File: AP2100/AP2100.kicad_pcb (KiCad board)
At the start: 6 copper layers, 150 x 150 mm, 73 parts, among them IC1 FDS86242, J1 Bus_PCI_Express_Mini, J2 Bus_PCI_Express_Mini, J3 Bus_PCI_Express_Mini, Q1 HMHA2801AR2, U1 TPS23751PWP, U2 TL431DBV, U3 LS1043ASE7KQB, U4 MPQ8634AGLE-P, U5 MPQ8634AGLE-P

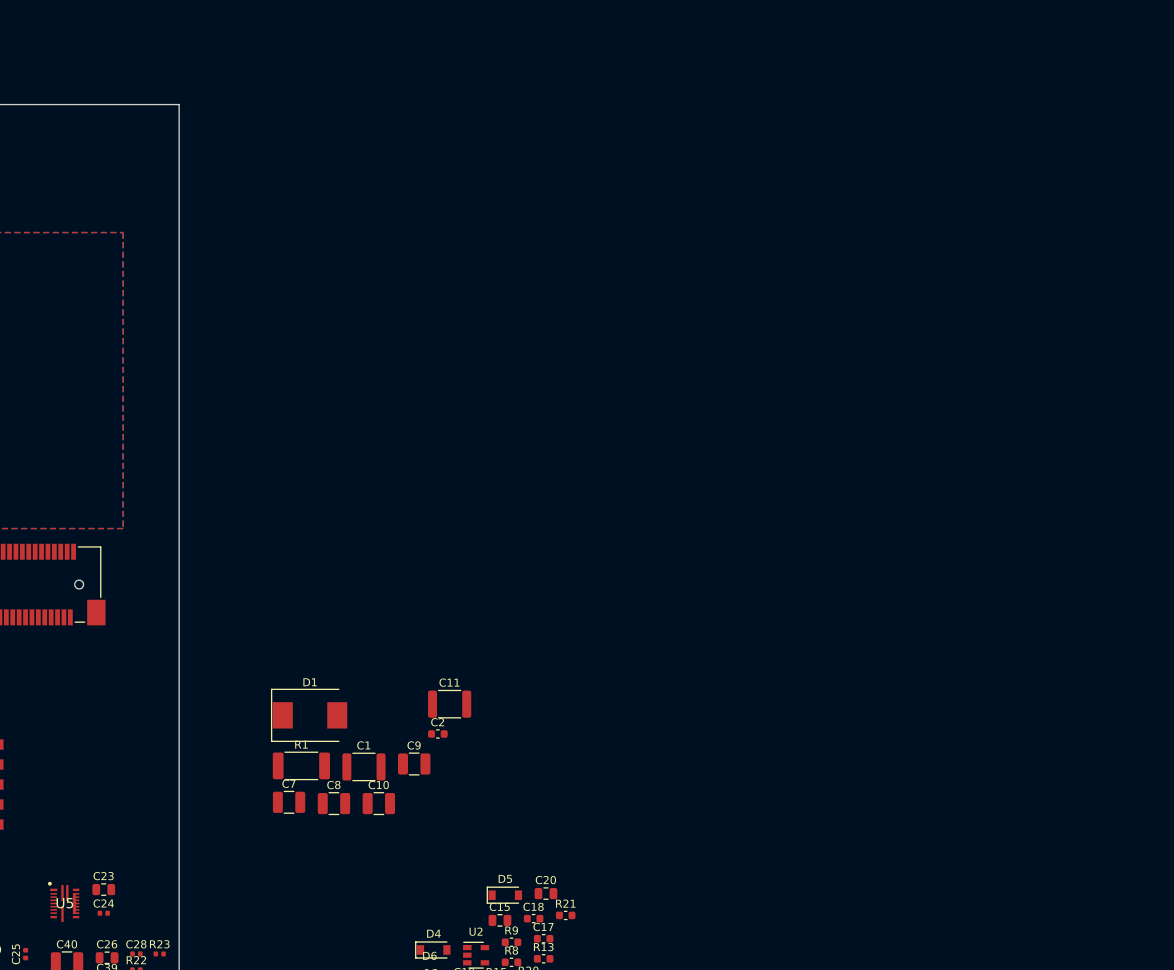
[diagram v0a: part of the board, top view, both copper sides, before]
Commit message: Update PoE section - almost done
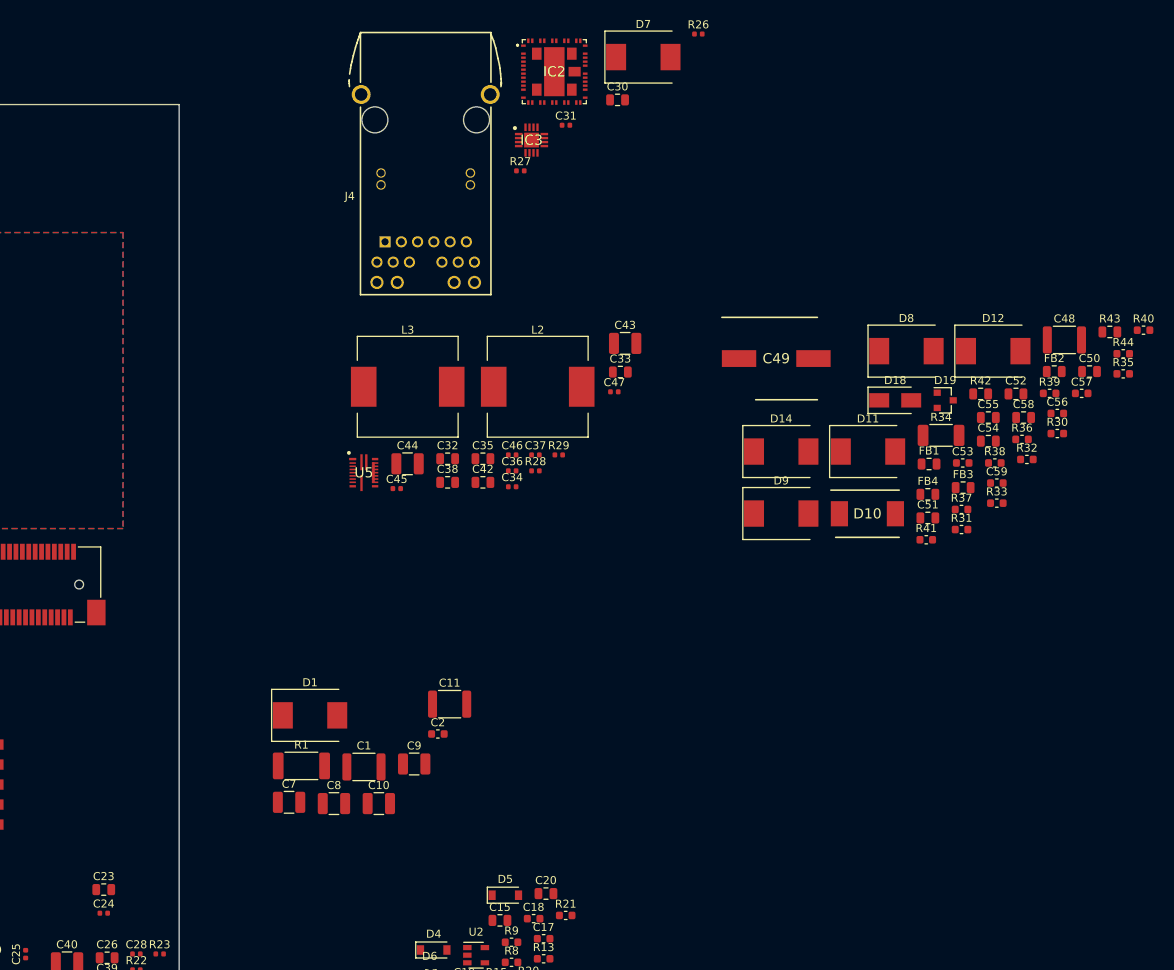
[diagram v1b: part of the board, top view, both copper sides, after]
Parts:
- added C30: 1nF 250V, Capacitor_SMD:C_0805_2012Metric, F.Cu at (204.8, -0.58)
- added C31: .1, Capacitor_SMD:C_0402_1005Metric, F.Cu at (198.4, 2.59)
- added C32: 22uF, Capacitor_SMD:C_0805_2012Metric, F.Cu at (183.6, 44.3)
- added C33: 22uF, Capacitor_SMD:C_0805_2012Metric, F.Cu at (205.2, 33.4)
- added C34: 500pF, Capacitor_SMD:C_0402_1005Metric, F.Cu at (191.6, 47.8)
- added C35: 22uF, Capacitor_SMD:C_0805_2012Metric, F.Cu at (188.0, 44.3)
- added C36: .1uF, Capacitor_SMD:C_0402_1005Metric, F.Cu at (191.6, 45.8)
- added C37: .1uF, Capacitor_SMD:C_0402_1005Metric, F.Cu at (194.5, 43.8)
- added C38: 22uF, Capacitor_SMD:C_0805_2012Metric, F.Cu at (183.6, 47.2)
- added C42: 22uF, Capacitor_SMD:C_0805_2012Metric, F.Cu at (188.0, 47.2)
- added C43: 100uF, Capacitor_SMD:C_1210_3225Metric, F.Cu at (205.8, 29.9)
- added C44: 100uF, Capacitor_SMD:C_1210_3225Metric, F.Cu at (178.6, 44.9)
- added C45: .1uF, Capacitor_SMD:C_0402_1005Metric, F.Cu at (177.2, 48.0)
- added C46: .1uF, Capacitor_SMD:C_0402_1005Metric, F.Cu at (191.6, 43.8)
- added C47: .1uF, Capacitor_SMD:C_0402_1005Metric, F.Cu at (204.4, 35.9)
- added C48: 2.2nF 2KV, Capacitor_SMD:C_1812_4532Metric, F.Cu at (260.7, 29.4)
- added C49: EEEFK2A330P, LIB_EEEFK2A330P:CAPAE1030X1050N, F.Cu at (224.6, 31.8)
- added C50: 1nF 250V, Capacitor_SMD:C_0805_2012Metric, F.Cu at (263.8, 33.4)
- added C51: 33nF 100V, Capacitor_SMD:C_0805_2012Metric, F.Cu at (243.6, 51.7)
- added C52: 33nF 100V, Capacitor_SMD:C_0805_2012Metric, F.Cu at (254.6, 36.2)
- added C53: 1nF, Capacitor_SMD:C_0603_1608Metric, F.Cu at (247.9, 44.8)
- added C54: 33nF 100V, Capacitor_SMD:C_0805_2012Metric, F.Cu at (251.1, 42.1)
- added C55: 33nF 100V, Capacitor_SMD:C_0805_2012Metric, F.Cu at (251.1, 39.1)
- added C56: 10nF 100V, Capacitor_SMD:C_0603_1608Metric, F.Cu at (259.8, 38.6)
- added C57: 10nF 100V, Capacitor_SMD:C_0603_1608Metric, F.Cu at (262.8, 36.1)
- added C58: 10nF 100V, Capacitor_SMD:C_0805_2012Metric, F.Cu at (255.6, 39.1)
- added C59: 10nF 100V, Capacitor_SMD:C_0603_1608Metric, F.Cu at (252.2, 47.3)
- added D10: STPS4S200S, LIB_STPS4S200S:DIOM8059X265N, F.Cu at (236.0, 51.1)
- added D11: SM15T68CA, Diode_SMD:D_SMC, F.Cu at (236.1, 43.4)
- added D12: SM15T68CA, Diode_SMD:D_SMC, F.Cu at (251.8, 30.8)
- added D14: SM15T68CA, Diode_SMD:D_SMC, F.Cu at (225.3, 43.4)
- added D18: SMAJ58A, Diode_SMD:D_SMA, F.Cu at (239.5, 37.0)
- added D19: BAV70, Package_TO_SOT_SMD:SOT-23, F.Cu at (245.8, 37.0)
- added D7: SM15T68CA, Diode_SMD:D_SMC, F.Cu at (208.0, -5.93)
- added D8: SM15T68CA, Diode_SMD:D_SMC, F.Cu at (240.9, 30.8)
- added D9: SM15T68CA, Diode_SMD:D_SMC, F.Cu at (225.3, 51.1)
- added FB1: 220 OHM, Inductor_SMD:L_0805_2012Metric, F.Cu at (243.7, 44.9)
- added FB2: 220 OHM, Inductor_SMD:L_0805_2012Metric, F.Cu at (259.4, 33.4)
- added FB3: 220 OHM, Inductor_SMD:L_0805_2012Metric, F.Cu at (248.0, 47.9)
- added FB4: 220 OHM, Inductor_SMD:L_0805_2012Metric, F.Cu at (243.6, 48.7)
- added IC2: PM8805TR, PM8805TR:PM8805TR, F.Cu at (196.9, -4.11)
- added IC3: PM8804TR, PM8804TR:QFN50P340X340X90-17N, F.Cu at (194.0, 4.44)
- added J4: 0826-1X1T-GH-F, 0826-1X1T-GH-F:BEL_0826-1X1T-GH-F, F.Cu at (180.8, 1.92)
- added L2: .56uH, Scott:L_13.5x12.5mm_H6mm, F.Cu at (194.8, 35.3)
- added L3: .56uH, Scott:L_13.5x12.5mm_H6mm, F.Cu at (178.6, 35.3)
- added R26: 30.1K, Resistor_SMD:R_0402_1005Metric, F.Cu at (214.9, -8.81)
- added R27: 6.98K, Resistor_SMD:R_0402_1005Metric, F.Cu at (192.7, 8.29)
- added R28: 30.1K, Resistor_SMD:R_0402_1005Metric, F.Cu at (194.5, 45.8)
- added R29: 6.98K, Resistor_SMD:R_0402_1005Metric, F.Cu at (197.5, 43.8)
- added R30: 75, Resistor_SMD:R_0603_1608Metric, F.Cu at (259.8, 41.1)
- added R31: 75, Resistor_SMD:R_0603_1608Metric, F.Cu at (247.8, 53.1)
- added R32: 75, Resistor_SMD:R_0603_1608Metric, F.Cu at (256.0, 44.4)
- added R33: 75, Resistor_SMD:R_0603_1608Metric, F.Cu at (252.2, 49.8)
- added R34: 0, Resistor_SMD:R_2010_5025Metric, F.Cu at (245.2, 41.4)
- added R35: 4.7K, Resistor_SMD:R_0603_1608Metric, F.Cu at (268.0, 33.7)
- added R36: 100K, Resistor_SMD:R_0603_1608Metric, F.Cu at (255.4, 41.9)
- added R37: 10K, Resistor_SMD:R_0603_1608Metric, F.Cu at (247.8, 50.6)
- added R38: 3.9K, Resistor_SMD:R_0603_1608Metric, F.Cu at (252.0, 44.8)
- added R39: 3.9K, Resistor_SMD:R_0603_1608Metric, F.Cu at (258.8, 36.1)
- added R40: 3.9K, Resistor_SMD:R_0603_1608Metric, F.Cu at (270.5, 28.2)
- added R41: 10K, Resistor_SMD:R_0603_1608Metric, F.Cu at (243.4, 54.4)
- added R42: 36.5, Resistor_SMD:R_0805_2012Metric, F.Cu at (250.2, 36.2)
- added R43: 150, Resistor_SMD:R_0805_2012Metric, F.Cu at (266.3, 28.4)
- added R44: 26.1K, Resistor_SMD:R_0603_1608Metric, F.Cu at (268.0, 31.2)
- moved U5 65.6 mm to (173.1, 46.0)
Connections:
- net /Power/+12V renamed 12V
- net /Power/CPU_VDD renamed CPU_VDD
- net /Power/EN_VDD renamed EN_VDD
- net Net-(U4-Pad9) renamed CPU_VDD_PG
- net Net-(U5-Pad8) renamed EN_3V3
- net Net-(U5-Pad9) renamed 3V3_PG
- C10 pad 2: GND -> CPU_GND_SENSE
- C11 pad 2: GND -> CPU_GND_SENSE
- C20 pad 2: GND -> CPU_GND_SENSE
- C21 pad 2: GND -> CPU_GND_SENSE
- C22 pad 2: GND -> CPU_GND_SENSE
- C23 pad 2: GND -> CPU_GND_SENSE
- C25 pad 1: GND -> CPU_GND_SENSE
- C26 pad 1: GND -> CPU_GND_SENSE
- C27 pad 2: GND -> CPU_GND_SENSE
- C28 pad 2: GND -> CPU_GND_SENSE
- C29 pad 1: GND -> CPU_GND_SENSE
- C39 pad 1: GND -> CPU_GND_SENSE
- C40 pad 1: GND -> CPU_GND_SENSE
- C41 pad 1: GND -> CPU_GND_SENSE
- C7 pad 2: GND -> CPU_GND_SENSE
- C8 pad 2: GND -> CPU_GND_SENSE
- C9 pad 2: GND -> CPU_GND_SENSE
- R21 pad 1: GND -> CPU_GND_SENSE
- R22 pad 2: GND -> CPU_GND_SENSE
- R23 pad 1: GND -> CPU_GND_SENSE
- TR1 pad 10: GND -> CPU_GND_SENSE
- TR1 pad 9: GND -> CPU_GND_SENSE
- U2 pad 5: GND -> CPU_GND_SENSE
- U4 pad 11: GND -> CPU_GND_SENSE
- U4 pad 12: GND -> CPU_GND_SENSE
- U4 pad 13: GND -> CPU_GND_SENSE
- U4 pad 14: GND -> CPU_GND_SENSE
- U4 pad 15: GND -> CPU_GND_SENSE
- U4 pad 16: GND -> CPU_GND_SENSE
- U4 pad 17: GND -> CPU_GND_SENSE
- U4 pad 18: GND -> CPU_GND_SENSE
- U4 pad 2: GND -> CPU_GND_SENSE
- U4 pad 6: GND -> CPU_GND_SENSE
- U5 pad 11: GND -> CPU_GND_SENSE
- U5 pad 12: GND -> CPU_GND_SENSE
- U5 pad 13: GND -> CPU_GND_SENSE
- U5 pad 14: GND -> CPU_GND_SENSE
- U5 pad 15: GND -> CPU_GND_SENSE
- U5 pad 16: GND -> CPU_GND_SENSE
- U5 pad 17: GND -> CPU_GND_SENSE
- U5 pad 18: GND -> CPU_GND_SENSE
- U5 pad 2: GND -> CPU_GND_SENSE
- U5 pad 6: Net-(U5-Pad6) -> CPU_GND_SENSE
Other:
- net class Default removed

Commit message: Add partsbox.io bom generator script
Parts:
- added C1: 10nF 25V, Capacitor_SMD:C_0603_1608Metric, F.Cu at (-554.7, -455.1)
- added C10: 100nF 25V, Capacitor_SMD:C_0603_1608Metric, F.Cu at (-539.2, -471.4)
- added C11: 100nF, Capacitor_SMD:C_0603_1608Metric, F.Cu at (-544.9, -466.8)
- added C12: 2.2uF 25V, Capacitor_SMD:C_0603_1608Metric, F.Cu at (-571.6, -439.5)
- added C13: 4.7uF, Capacitor_SMD:C_1210_3225Metric, F.Cu at (-592.3, -438.8)
- added C14: 100nF 25V, Capacitor_SMD:C_0603_1608Metric, F.Cu at (-555.4, -460.1)
- added C15: 100nF 25V, Capacitor_SMD:C_0603_1608Metric, F.Cu at (-577.4, -438.0)
- added C16: EEEFK2A330P, LIB_EEEFK2A330P:CAPAE1030X1050N, F.Cu at (-577.2, -476.8)
- added C17: 4.7uF, Capacitor_SMD:C_1210_3225Metric, F.Cu at (-570.2, -457.1)
- added C18: 4.7uF, Capacitor_SMD:C_1210_3225Metric, F.Cu at (-586.2, -442.2)
- added C19: 2.2uF 25V, Capacitor_SMD:C_0603_1608Metric, F.Cu at (-532.2, -476.8)
- added C2: 4.7uF, Capacitor_SMD:C_1210_3225Metric, F.Cu at (-551.1, -474.6)
- added C20: 4.7uF, Capacitor_SMD:C_1210_3225Metric, F.Cu at (-545.4, -481.0)
- added C3: 4.7uF, Capacitor_SMD:C_1210_3225Metric, F.Cu at (-564.6, -458.3)
- added C31: 22nF, Capacitor_SMD:C_0603_1608Metric, F.Cu at (-571.4, -442.0)
- added C4: 100pF 25V, Capacitor_SMD:C_0603_1608Metric, F.Cu at (-558.7, -453.4)
- added C5: 2.2nF 2KV, Capacitor_SMD:C_1812_4532Metric, F.Cu at (-557.4, -474.0)
- added C6: 2.2nF 2KV, Capacitor_SMD:C_1812_4532Metric, F.Cu at (-598.6, -438.4)
- added C60: 47nF 200V, Capacitor_SMD:C_1206_3216Metric, F.Cu at (-577.8, -454.0)
- added C61: 100pF 50V, Capacitor_SMD:C_0805_2012Metric, F.Cu at (-579.3, -446.7)
- added C62: 2200pF 2KV, Capacitor_SMD:C_1812_4532Metric, F.Cu at (-564.5, -467.1)
- added C63: 100nF 25V, Capacitor_SMD:C_0603_1608Metric, F.Cu at (-554.7, -457.6)
- added C64: 220pF, Capacitor_SMD:C_0603_1608Metric, F.Cu at (-531.9, -479.3)
- added C65: 100pF 50V, Capacitor_SMD:C_0805_2012Metric, F.Cu at (-575.6, -443.7)
- added C66: 1nF, Capacitor_SMD:C_0805_2012Metric, F.Cu at (-559.6, -458.7)
- added C67: 47uF 16V, Capacitor_SMD:C_1210_3225Metric, F.Cu at (-580.6, -442.2)
- added C68: 47uF 16V, Capacitor_SMD:C_1210_3225Metric, F.Cu at (-564.6, -462.5)
- added C69: EEEFK1C101P, Capacitor_SMD:CP_Elec_6.3x5.9, F.Cu at (-579.7, -466.5)
- added C7: 1nF, Capacitor_SMD:C_0805_2012Metric, F.Cu at (-567.2, -453.5)
- added C70: 47uF 16V, Capacitor_SMD:C_1210_3225Metric, F.Cu at (-577.8, -450.3)
- added C71: 47uF 16V, Capacitor_SMD:C_1210_3225Metric, F.Cu at (-558.2, -465.2)
- added C72: 47uF 16V, Capacitor_SMD:C_1210_3225Metric, F.Cu at (-586.7, -438.0)
- added C8: 1nF, Capacitor_SMD:C_0805_2012Metric, F.Cu at (-553.2, -465.8)
- added C9: 1nF, Capacitor_SMD:C_0805_2012Metric, F.Cu at (-546.1, -472.5)
- added D1: SMAJ58A, Diode_SMD:D_SMA, F.Cu at (-606.1, -438.6)
- added D13: AUX, LED_SMD:LED_0603_1608Metric, F.Cu at (431.8, -25.4)
- added D15: T2, LED_SMD:LED_0603_1608Metric, F.Cu at (435.9, -30.6)
- added D16: T1, LED_SMD:LED_0603_1608Metric, F.Cu at (431.8, -28.0)
- added D17: T0, LED_SMD:LED_0603_1608Metric, F.Cu at (431.8, -30.6)
- added D2: BAS16J, Diode_SMD:D_SOD-323, F.Cu at (-536.0, -481.6)
- added D20: BAS70, Diode_SMD:D_SOD-323, F.Cu at (-547.3, -469.5)
- added D21: BAS16J, Diode_SMD:D_SOD-323, F.Cu at (-562.8, -454.7)
- added D22: BZX84C10, Package_TO_SOT_SMD:SOT-23, F.Cu at (-551.7, -470.2)
- added D23: BAS16J, Diode_SMD:D_SOD-323, F.Cu at (-553.2, -462.9)
- added D24: BZX84C10, Package_TO_SOT_SMD:SOT-23, F.Cu at (-581.7, -437.8)
- added D25: +12V, LED_SMD:LED_0603_1608Metric, F.Cu at (435.9, -28.0)
- added D3: BAS70, Diode_SMD:D_SOD-323, F.Cu at (-571.3, -444.8)
- added D4: BAS16J, Diode_SMD:D_SOD-323, F.Cu at (-541.4, -474.1)
- added D5: BAS16J, Diode_SMD:D_SOD-323, F.Cu at (-582.9, -460.9)
- added D6: BAS70, Diode_SMD:D_SOD-323, F.Cu at (-575.7, -440.8)
- added J5: Barrel_Jack, Connector_BarrelJack:BarrelJack_Horizontal, F.Cu at (427.2, -26.5)
- added L1: 1mH, Inductor_SMD:L_Wuerth_HCI-5040, F.Cu at (-585.3, -447.7)
- added L4: 5.6uH, Inductor_SMD:L_Wuerth_HCI-5040, F.Cu at (-576.8, -459.0)
- added L5: 7443631000, LIB_7443631000:WE-HCF_201322, F.Cu at (-597.5, -470.5)
- added Q1: FOD817AS, LIB_FOD817AS:SOP254P1016X385-4N, F.Cu at (-563.0, -479.8)
- added Q2: BSC190N15NS3GATMA1, LIB_BSC190N15NS3GATMA1:PG-TDSON-8_1, F.Cu at (-552.7, -479.9)
- added Q3: FDMC86259P, LIB_FDMC86259P:FDMC86160, F.Cu at (-571.1, -466.2)
- added Q4: PBSS4240T, Package_TO_SOT_SMD:SOT-23, F.Cu at (-540.4, -480.8)
- added Q5: PBSS4240T, Package_TO_SOT_SMD:SOT-23, F.Cu at (-572.7, -448.5)
- added R1: 91K, Resistor_SMD:R_0603_1608Metric, F.Cu at (-567.2, -445.3)
- added R10: 10K, Resistor_SMD:R_0603_1608Metric, F.Cu at (-549.0, -466.7)
- added R11: 0R05, Resistor_SMD:R_1210_3225Metric, F.Cu at (-572.2, -452.9)
- added R12: R100, Resistor_SMD:R_1210_3225Metric, F.Cu at (-558.1, -469.4)
- added R13: 47K, Resistor_SMD:R_0603_1608Metric, F.Cu at (-549.1, -463.1)
- added R14: 2K, Resistor_SMD:R_0603_1608Metric, F.Cu at (-558.9, -450.9)
- added R15: 1K, Resistor_SMD:R_0603_1608Metric, F.Cu at (-563.2, -445.3)
- added R16: 4.7K, Resistor_SMD:R_0603_1608Metric, F.Cu at (-568.5, -447.8)
- added R17: 0, Resistor_SMD:R_0603_1608Metric, F.Cu at (-537.1, -476.4)
- added R18: 22, Resistor_SMD:R_0603_1608Metric, F.Cu at (-545.1, -464.2)
- added R19: 0, Resistor_SMD:R_0603_1608Metric, F.Cu at (-562.9, -452.0)
- added R2: 330K, Resistor_SMD:R_0603_1608Metric, F.Cu at (-564.5, -447.8)
- added R20: 20K, Resistor_SMD:R_0603_1608Metric, F.Cu at (-531.9, -481.8)
- added R21: 5.23K, Resistor_SMD:R_0603_1608Metric, F.Cu at (-527.9, -481.8)
- added R24: 10K, Resistor_SMD:R_0603_1608Metric, F.Cu at (443.9, -28.1)
- added R25: 3.74K, Resistor_SMD:R_0603_1608Metric, F.Cu at (443.9, -30.6)
- added R26: 10K, Resistor_SMD:R_0603_1608Metric, F.Cu at (-573.4, -437.0)
- added R27: 1K, Resistor_SMD:R_0603_1608Metric, F.Cu at (-550.7, -457.6)
- added R3: 10K, Resistor_SMD:R_0603_1608Metric, F.Cu at (-551.4, -460.1)
- added R4: 130K, Resistor_SMD:R_0603_1608Metric, F.Cu at (-536.2, -478.9)
- added R45: 22, Resistor_SMD:R_0603_1608Metric, F.Cu at (-567.2, -442.8)
- added R46: 10K, Resistor_SMD:R_0603_1608Metric, F.Cu at (-558.7, -455.9)
- added R47: 18, Resistor_SMD:R_0805_2012Metric, F.Cu at (-541.3, -477.1)
- added R48: 10K, Resistor_SMD:R_0603_1608Metric, F.Cu at (-537.3, -473.9)
- added R5: 2K, Resistor_SMD:R_0603_1608Metric, F.Cu at (-543.2, -469.7)
- added R6: 0, Resistor_SMD:R_1206_3216Metric, F.Cu at (-570.2, -460.9)
- added R7: 390, Resistor_SMD:R_0603_1608Metric, F.Cu at (-560.5, -448.4)
- added R8: 10, Resistor_SMD:R_0805_2012Metric, F.Cu at (-559.6, -461.6)
- added R9: 10K, Resistor_SMD:R_0805_2012Metric, F.Cu at (-567.2, -450.6)
- added TR1: POE72PR-12ED, Scott:Transformer_Coilcraft_POE72PR, F.Cu at (-599.6, -449.4)
- added U1: TS2431-AILT, digikey-footprints:SOT-23-3, F.Cu at (-545.9, -476.4)
- added U2: STL90N6F7, Scott:TRANS_STL60P4LLF6, F.Cu at (-584.4, -454.5)
- added U6: STL90N6F7, Scott:TRANS_STL60P4LLF6, F.Cu at (-564.7, -473.0)
- C57: value 10nF 100V -> 10nF
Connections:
- C49 pad 2: Net-(C49-Pad2) -> GNDPWR
- C57 pad 1: Net-(C57-Pad1) -> GNDPWR
- C57 pad 2: GNDPWR -> Net-(C57-Pad2)
- IC2 pad 24: Net-(C57-Pad1) -> Net-(C57-Pad2)
- IC3 pad 1: Net-(IC3-Pad1) -> CPU_GND_SENSE
- IC3 pad 10: Net-(IC3-Pad10) -> GNDPWR
- IC3 pad 6: Net-(IC3-Pad6) -> /PoE Power/PGD
- IC3 pad 9: Net-(IC3-Pad9) -> Net-(D2-Pad1)

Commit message: Add PartsBox part numbers to everything so far
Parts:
- C1: renamed from C21; footprint Capacitor_SMD:C_0805_2012Metric -> Capacitor_SMD:C_1210_3225Metric
- C10: renamed from C27; value .1 -> .1uF; footprint Capacitor_SMD:C_0402_1005Metric -> Capacitor_SMD:C_0603_1608Metric
- C11: renamed from C28; footprint Capacitor_SMD:C_0402_1005Metric -> Capacitor_SMD:C_0603_1608Metric
- C12: renamed from C29; footprint Capacitor_SMD:C_0402_1005Metric -> Capacitor_SMD:C_0603_1608Metric
- C13: renamed from C32; footprint Capacitor_SMD:C_0805_2012Metric -> Capacitor_SMD:C_1210_3225Metric
- C14: renamed from C33; footprint Capacitor_SMD:C_0805_2012Metric -> Capacitor_SMD:C_1210_3225Metric
- C15: renamed from C35; footprint Capacitor_SMD:C_0805_2012Metric -> Capacitor_SMD:C_1210_3225Metric
- C16: renamed from C36; footprint Capacitor_SMD:C_0402_1005Metric -> Capacitor_SMD:C_0603_1608Metric
- C17: renamed from C37; footprint Capacitor_SMD:C_0402_1005Metric -> Capacitor_SMD:C_0603_1608Metric
- C18: renamed from C38; footprint Capacitor_SMD:C_0805_2012Metric -> Capacitor_SMD:C_1210_3225Metric
- C19: renamed from C42; footprint Capacitor_SMD:C_0805_2012Metric -> Capacitor_SMD:C_1210_3225Metric
- C2: renamed from C22; footprint Capacitor_SMD:C_0805_2012Metric -> Capacitor_SMD:C_1210_3225Metric
- C20: renamed from C43; value 100uF -> 47uF
- C21: renamed from C44; value 100uF -> 47uF
- C22: renamed from C34; footprint Capacitor_SMD:C_0402_1005Metric -> Capacitor_SMD:C_0603_1608Metric
- C23: renamed from C45; footprint Capacitor_SMD:C_0402_1005Metric -> Capacitor_SMD:C_0603_1608Metric
- C24: renamed from C46; footprint Capacitor_SMD:C_0402_1005Metric -> Capacitor_SMD:C_0603_1608Metric
- C25: renamed from C47; footprint Capacitor_SMD:C_0402_1005Metric -> Capacitor_SMD:C_0603_1608Metric
- C26: renamed from C30; value 1nF 250V -> 1nF
- C27: renamed from C51; value 33nF 100V -> 33nF
- C28: renamed from C54; value 33nF 100V -> 33nF
- C29: renamed from C50; value 1nF 250V -> 1nF
- C3: renamed from C23; footprint Capacitor_SMD:C_0805_2012Metric -> Capacitor_SMD:C_1210_3225Metric
- C30: renamed from C52; value 33nF 100V -> 33nF
- C31: renamed from C55; value 33nF 100V -> 33nF
- C32: renamed from C56; value 10nF 100V -> 10nF
- C33: renamed from C48; value 2.2nF 2KV -> 2.2nF
- C34: renamed from C59; value 10nF 100V -> 10nF
- C38: renamed from C5; value 2.2nF 2KV -> 2.2nF
- C4: renamed from C24; footprint Capacitor_SMD:C_0402_1005Metric -> Capacitor_SMD:C_0603_1608Metric
- C40: renamed from C3; value 4.7uF -> 100nF; footprint Capacitor_SMD:C_1210_3225Metric -> Capacitor_SMD:C_0805_2012Metric
- C47: renamed from C62; value 2200pF 2KV -> 2200pF
- C48: renamed from C6; value 2.2nF 2KV -> 2.2nF
- C5: renamed from C25; footprint Capacitor_SMD:C_0402_1005Metric -> Capacitor_SMD:C_0603_1608Metric
- C50: renamed from C58; value 10nF 100V -> 10nF
- C52: renamed from C15; value 100nF 25V -> 100nF
- C53: renamed from C65; value 100pF 50V -> 100pF
- C55: renamed from C67; value 47uF 16V -> 47uF
- C56: renamed from C68; value 47uF 16V -> 47uF
- C57: renamed from C70; value 47uF 16V -> 47uF
- C58: renamed from C72; value 47uF 16V -> 100nF; footprint Capacitor_SMD:C_1210_3225Metric -> Capacitor_SMD:C_0603_1608Metric
- C59: renamed from C61; value 100pF 50V -> 100pF
- C6: renamed from C26; footprint Capacitor_SMD:C_0805_2012Metric -> Capacitor_SMD:C_1210_3225Metric
- C62: renamed from C1; value 10nF 25V -> 10nF
- C63: renamed from C10; value 100nF 25V -> 100nF
- C64: renamed from C60; value 47nF 200V -> 47nF
- C65: renamed from C14; value 100nF 25V -> 100nF
- C66: renamed from C4; value 100pF 25V -> 100pF
- C67: renamed from C63; value 100nF 25V -> 100nF
- C7: renamed from C39; footprint Capacitor_SMD:C_0805_2012Metric -> Capacitor_SMD:C_1210_3225Metric
- C8: renamed from C40; value 100uF -> 47uF
- C9: renamed from C41; value 100uF -> 47uF
- R1: renamed from R22; footprint Resistor_SMD:R_0402_1005Metric -> Resistor_SMD:R_0603_1608Metric
- R2: renamed from R23; footprint Resistor_SMD:R_0402_1005Metric -> Resistor_SMD:R_0603_1608Metric
- R5: renamed from R28; footprint Resistor_SMD:R_0402_1005Metric -> Resistor_SMD:R_0603_1608Metric
- R6: renamed from R29; footprint Resistor_SMD:R_0402_1005Metric -> Resistor_SMD:R_0603_1608Metric
- renumbered C53 to C35, C49 to C36, C16 to C37, C2 to C39, C7 to C41, C9 to C42, C13 to C43, C17 to C44, C18 to C45, C20 to C46, C57 to C49, C12 to C51, C66 to C54, C69 to C60, C8 to C61, C64 to C68, C31 to C69, C19 to C70, C11 to C71, D7 to D1, D13 to D10, D10 to D11, D19 to D12, D1 to D13, D18 to D14, D5 to D15, D4 to D16, D25 to D17, D23 to D18, D21 to D19, D8 to D2, D24 to D20, D2 to D21, D3 to D23, D6 to D24, D20 to D25, D11 to D3, D14 to D4, D9 to D5, D12 to D6, D15 to D7, D16 to D8, D17 to D9, FB2 to FB1, FB3 to FB2, FB1 to FB3, IC2 to IC1, IC3 to IC2, L2 to L1, L3 to L2, L4 to L3, L1 to L4, Q5 to Q1, Q4 to Q3, Q3 to Q4, Q1 to Q5, R42 to R10, R33 to R11, R43 to R12, R44 to R13, R40 to R14, R39 to R15, R38 to R16, R34 to R17, R41 to R18, R36 to R19, R35 to R20, R37 to R21, R48 to R22, R27 to R23, R45 to R24, R3 to R25, R15 to R26, R18 to R27, R47 to R28, R46 to R29, R24 to R3, R1 to R30, R8 to R31, R2 to R32, R26 to R33, R9 to R34, R11 to R35, R12 to R36, R6 to R37, R19 to R38, R5 to R39, R25 to R4, R10 to R40, R17 to R41, R4 to R42, R14 to R43, R20 to R44, R13 to R45, R7 to R46, R16 to R47, R21 to R48, R30 to R7, R31 to R8, R32 to R9, U3 to U1, U4 to U2, U5 to U3, U6 to U4, U2 to U5, U1 to U6
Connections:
- C62 pad 1: CPU_GND_SENSE -> GNDA
- C66 pad 1: CPU_GND_SENSE -> GNDA
- C71 pad 1: CPU_GND_SENSE -> GNDA
- IC2 pad 1: CPU_GND_SENSE -> GNDA
- Q5 pad 3: CPU_GND_SENSE -> GNDA
- R30 pad 1: CPU_GND_SENSE -> GNDA
- R32 pad 1: CPU_GND_SENSE -> GNDA
- R37 pad 2: CPU_GND_SENSE -> GNDA
- R42 pad 1: CPU_GND_SENSE -> GNDA

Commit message: More work on memory
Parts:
- added IC3: AS4C256M16D4-75BINTR, LIB_AS4C256M16D4-75BINTR:BGA96C80P9X16_750X1350X120, F.Cu at (410.2, 31.4)
- added IC4: AS4C256M16D4-75BINTR, LIB_AS4C256M16D4-75BINTR:BGA96C80P9X16_750X1350X120, F.Cu at (399.6, 31.4)
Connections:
- C16 pad 1: Net-(C36-Pad1) -> Net-(C16-Pad1)
- C16 pad 2: Net-(C36-Pad2) -> Net-(C16-Pad2)
- C31 pad 1: Net-(C55-Pad1) -> Net-(C31-Pad1)
- C69 pad 1: Net-(C31-Pad1) -> Net-(C69-Pad1)
- C70 pad 1: Net-(C19-Pad1) -> Net-(C70-Pad1)
- D15 pad 2: Net-(D5-Pad2) -> Net-(D15-Pad2)
- D21 pad 1: Net-(D2-Pad1) -> Net-(D21-Pad1)
- D24 pad 2: Net-(C19-Pad1) -> Net-(C70-Pad1)
- D25 pad 1: Net-(C19-Pad1) -> Net-(C70-Pad1)
- FB3 pad 2: Net-(C55-Pad1) -> Net-(C31-Pad1)
- IC1 pad 33: Net-(C55-Pad1) -> Net-(C31-Pad1)
- IC1 pad 36: Net-(C55-Pad1) -> Net-(C31-Pad1)
- IC1 pad 37: Net-(C55-Pad1) -> Net-(C31-Pad1)
- IC1 pad EP2: Net-(C55-Pad1) -> Net-(C31-Pad1)
- IC2 pad 9: Net-(D2-Pad1) -> Net-(D21-Pad1)
- L2 pad 1: Net-(C36-Pad1) -> Net-(C16-Pad1)
- R31 pad 1: Net-(D2-Pad1) -> Net-(D21-Pad1)
- R45 pad 1: Net-(C19-Pad1) -> Net-(C70-Pad1)
- R47 pad 2: Net-(C31-Pad1) -> Net-(C69-Pad1)
- R5 pad 1: Net-(R28-Pad1) -> Net-(R5-Pad1)
- TR1 pad 4: Net-(D5-Pad2) -> Net-(D15-Pad2)
- U3 pad 1: Net-(C36-Pad2) -> Net-(C16-Pad2)
- U3 pad 20: Net-(C36-Pad1) -> Net-(C16-Pad1)
- U3 pad 4: Net-(R28-Pad1) -> Net-(R5-Pad1)
